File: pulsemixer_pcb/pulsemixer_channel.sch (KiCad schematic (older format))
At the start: 12 parts, among them SW501 Vol_Encoder, SW502 SW_MUTE, U501 MCP23017_SP

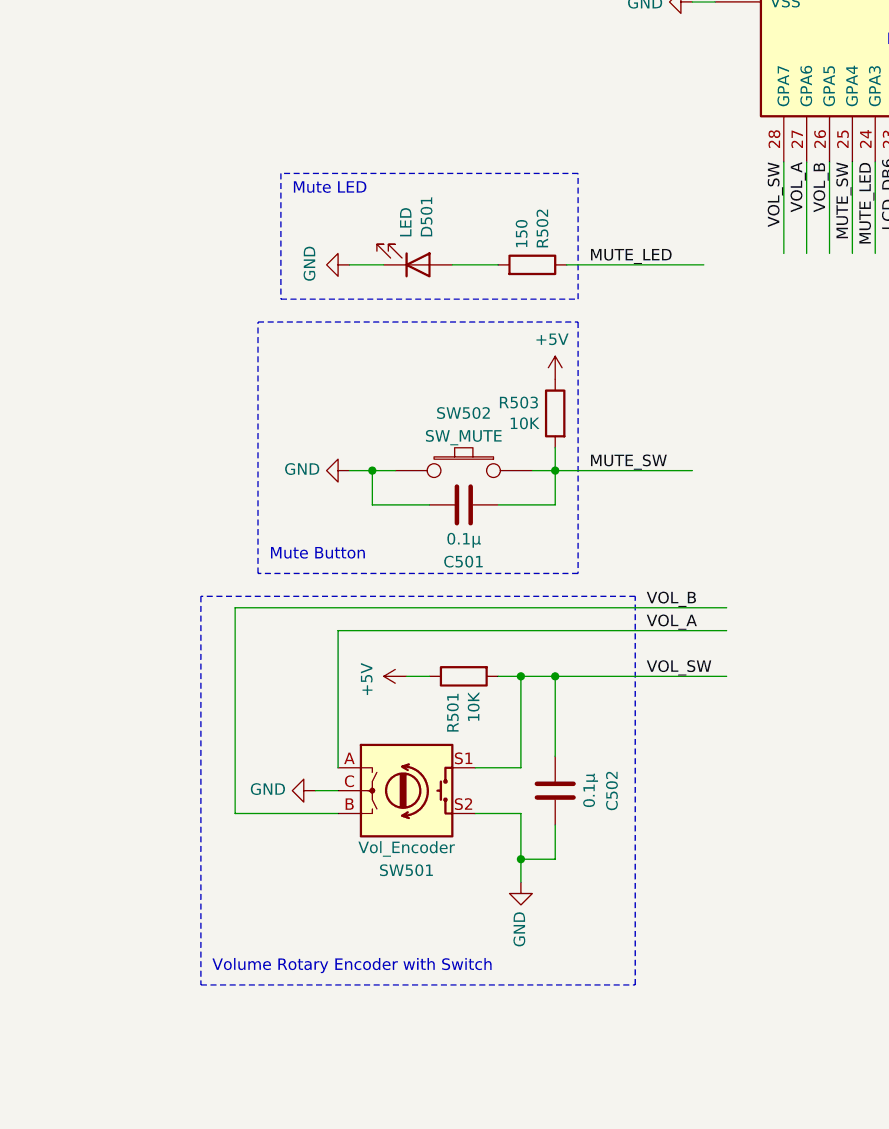
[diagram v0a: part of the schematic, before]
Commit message: Revised schematic after testing rotary encoder.
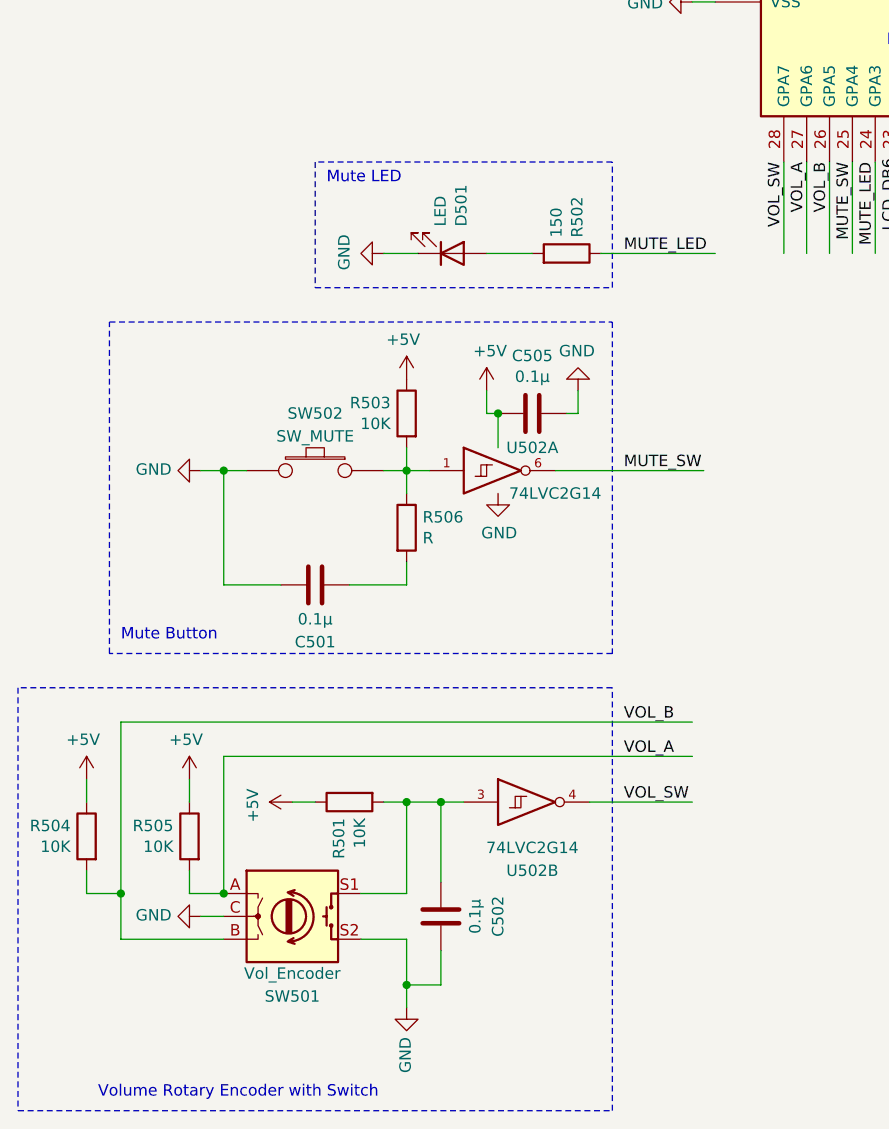
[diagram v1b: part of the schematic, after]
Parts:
- added C505: 0.1µ, symbol Device:C
- added R504, R505: 10K, Resistors_SMD:R_1206_HandSoldering, symbol Device:R
- added R506: R, symbol Device:R
- added U502: 74LVC2G14, symbol 74xGxx:74LVC2G14
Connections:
- wire segments 78 -> 93
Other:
- moved on the sheet: C501, C502, D501, R501, R502, R503, SW501, SW502

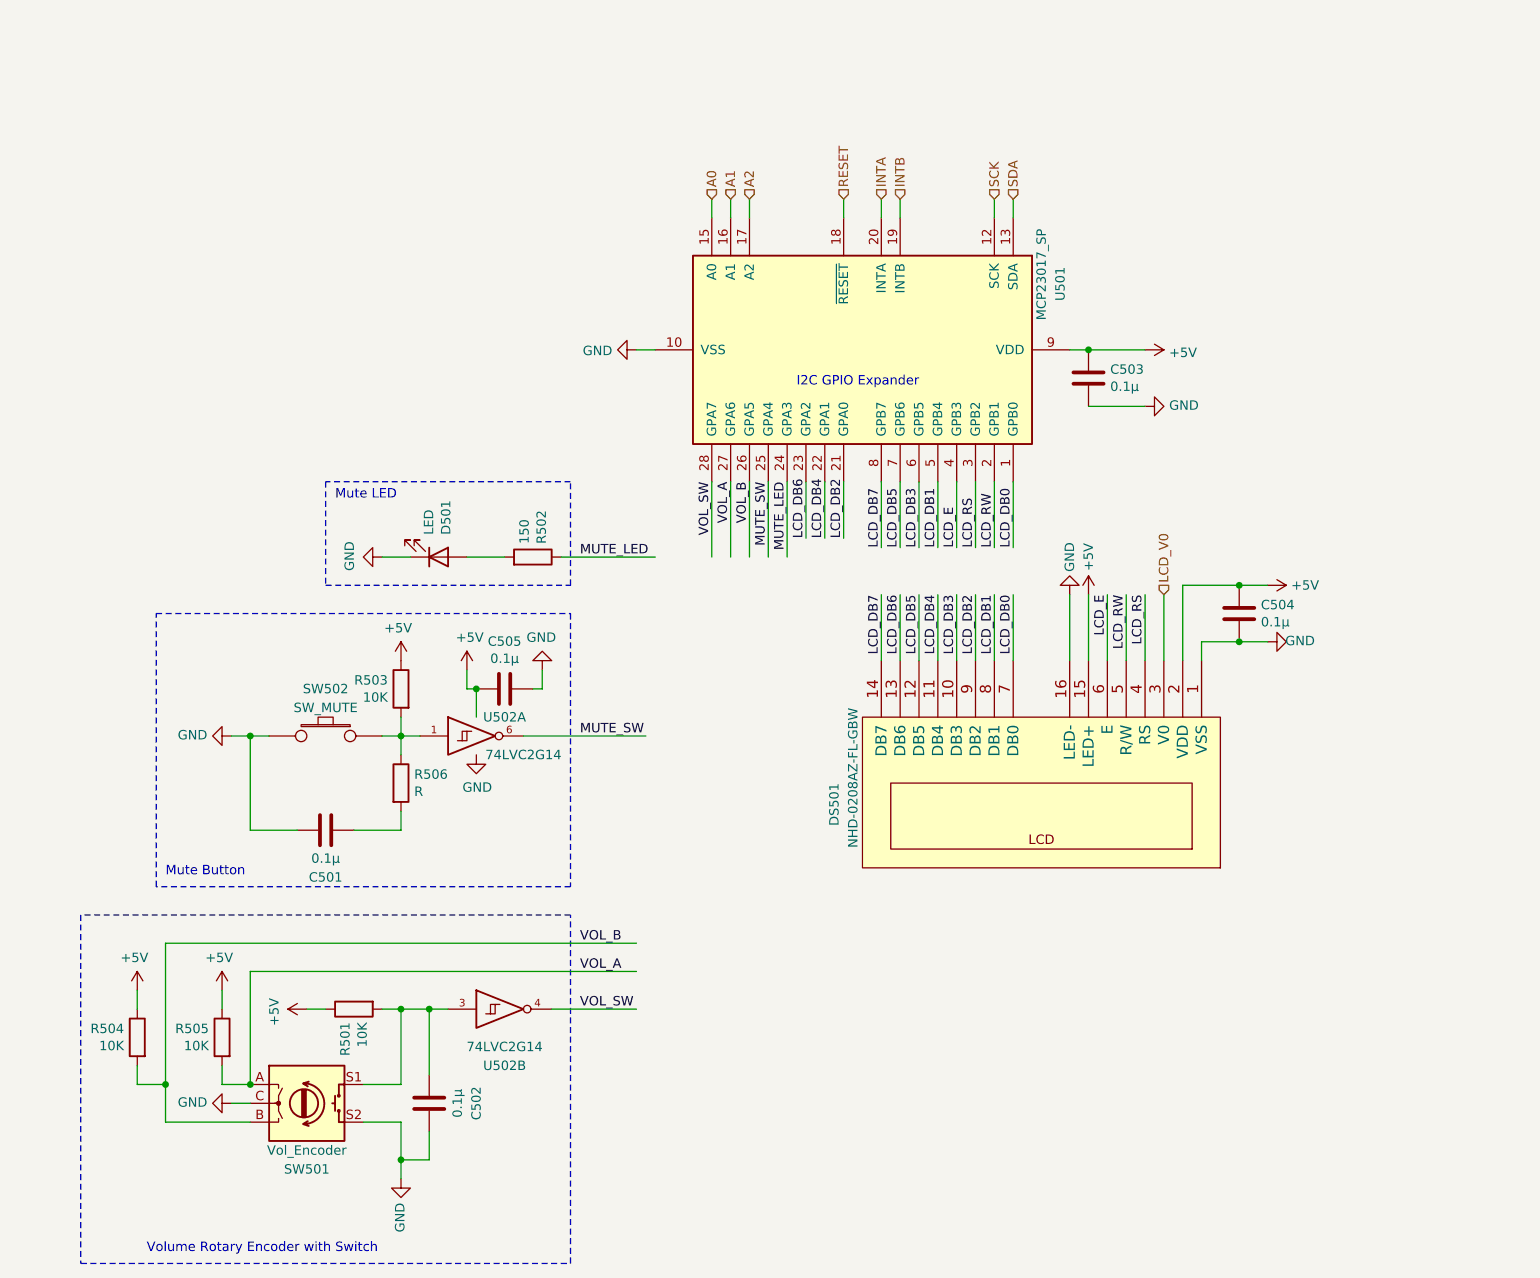
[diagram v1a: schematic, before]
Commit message: Simple reading of rotary encoder through the GPIO expander, with interrupts.
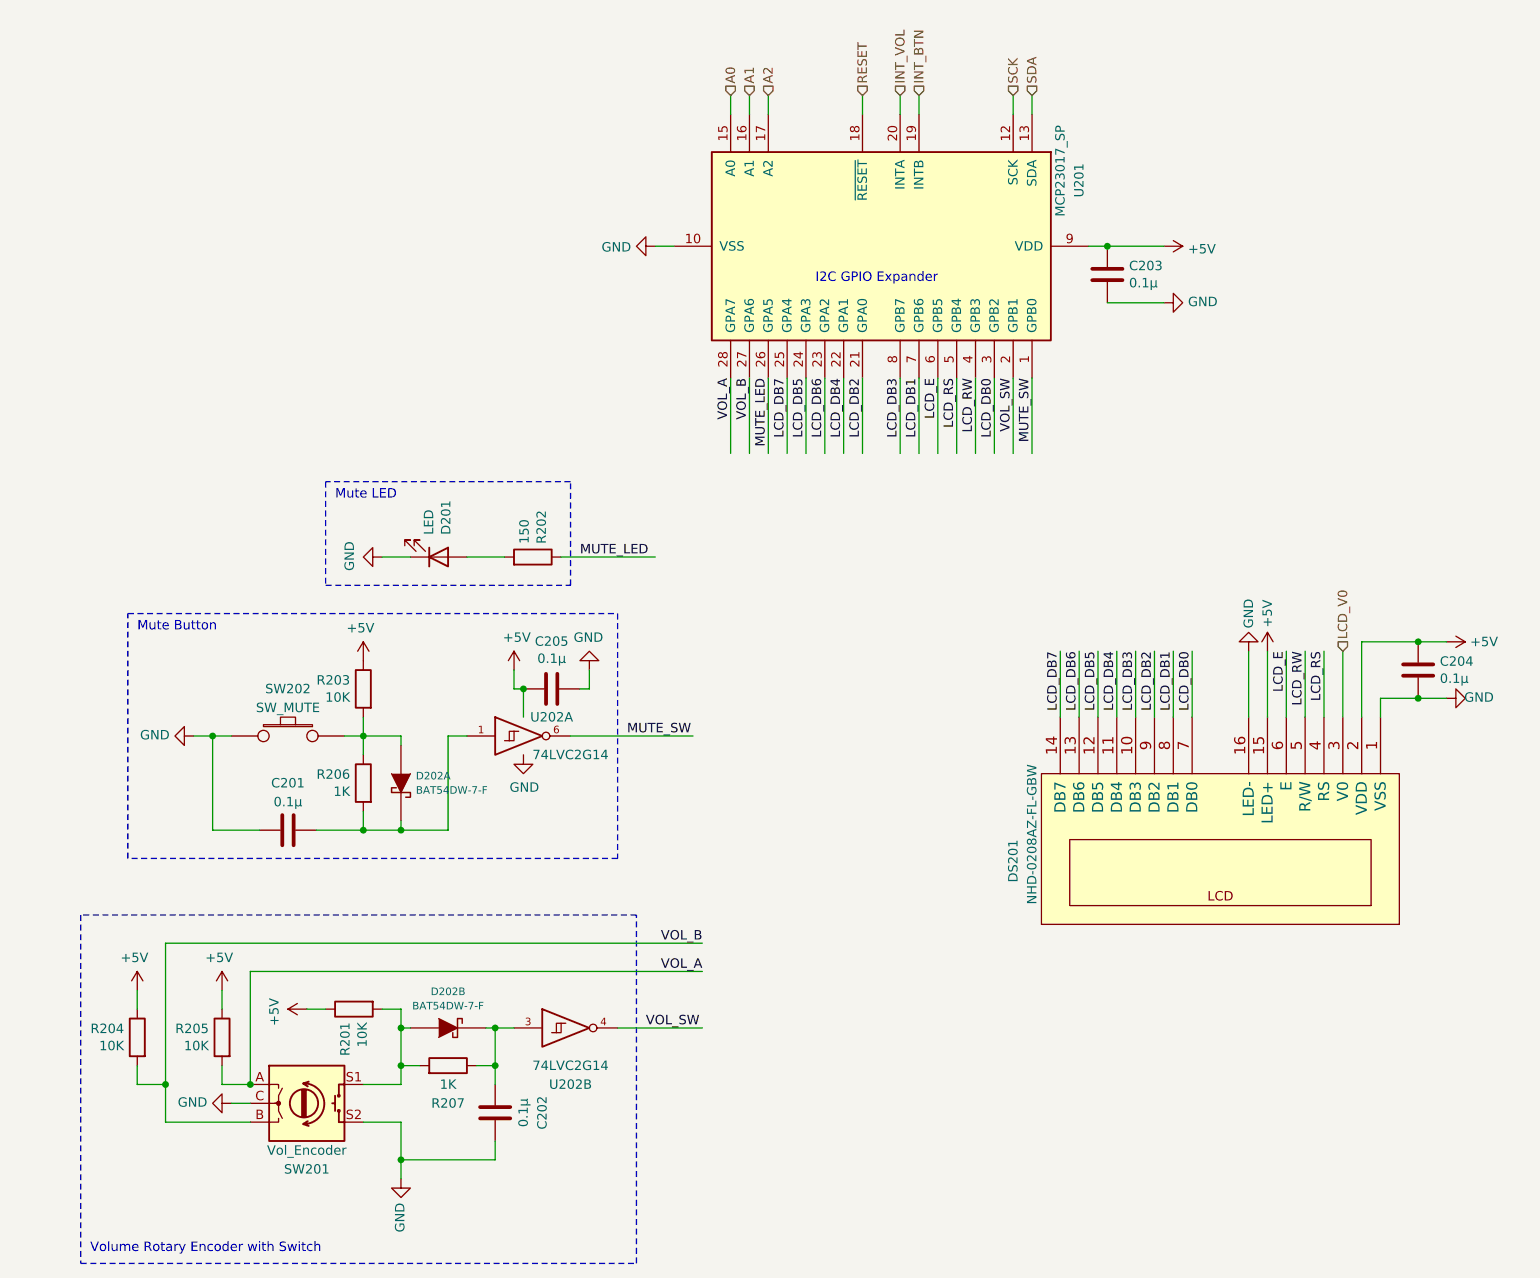
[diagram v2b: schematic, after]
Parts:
- added D502: BAT54DW-7-F, TO_SOT_Packages_SMD:SOT-23-6_Handsoldering, symbol pulsemixer_pcb:BAT54DW-7-F
- added R507: 1K, Resistors_SMD:R_1206_HandSoldering, symbol Device:R
- C505: footprint (none) -> Capacitors_SMD:C_0805_HandSoldering
- R506: value R -> 1K; footprint (none) -> Resistors_SMD:R_1206_HandSoldering
- U502: footprint (none) -> TO_SOT_Packages_SMD:SOT-23-6_Handsoldering
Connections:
- net labels added: INT_BTN, INT_VOL
- net labels removed: INTA, INTB
- wire segments 93 -> 105
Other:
- moved on the sheet: C201, C202, C203, C204, C205, DS201, R203, R206, SW202, U201, U202A, U202B

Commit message: Rearranged LCD pins to allow for interrupts on both GPIO banks.
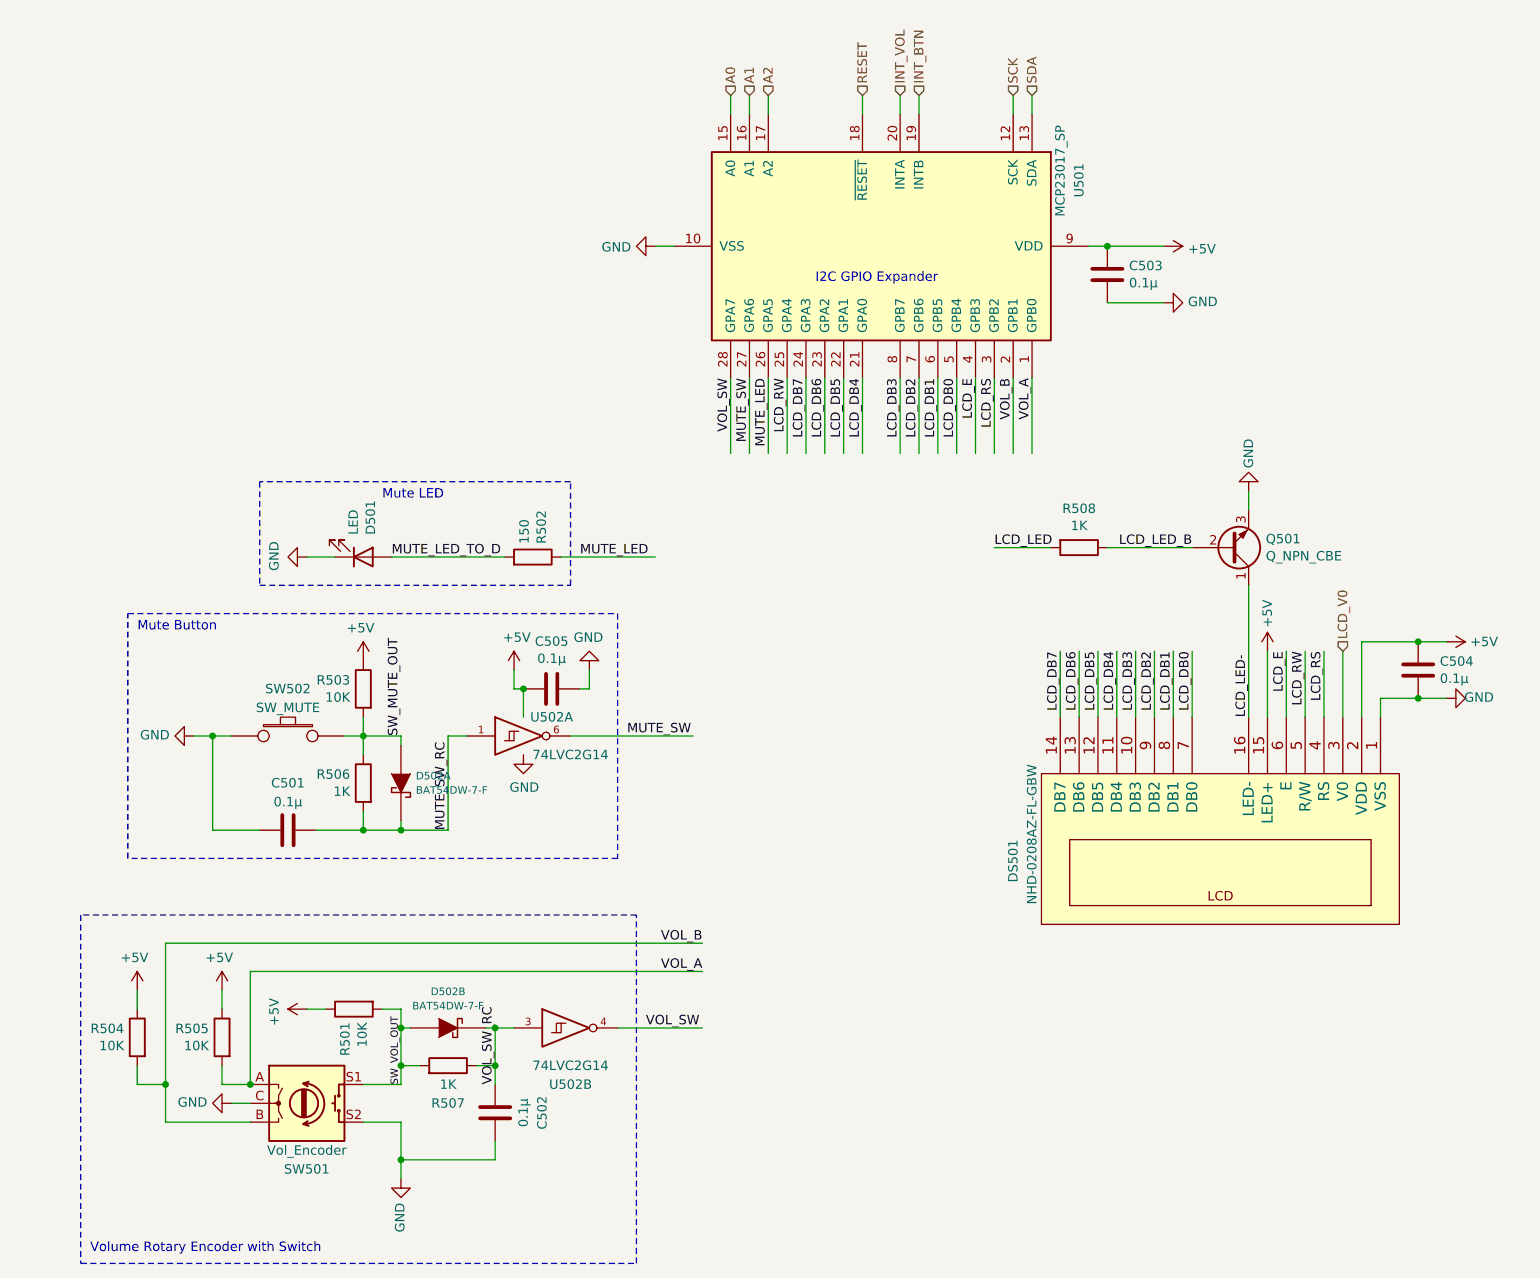
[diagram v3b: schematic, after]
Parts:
- added Q501: Q_NPN_CBE, TO_SOT_Packages_SMD:SOT-23_Handsoldering, symbol Device:Q_NPN_CBE
- added R508: 1K, Resistors_SMD:R_1206_HandSoldering, symbol Device:R
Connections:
- net labels added: LCD_LED, LCD_LED-, LCD_LED_B, MUTE_LED_TO_D, MUTE_SW_RC, SW_MUTE_OUT, SW_VOL_OUT, VOL_SW_RC
- wire segments 105 -> 108
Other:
- moved on the sheet: D501

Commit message: Firmware code to turn LCD backlight on and off.
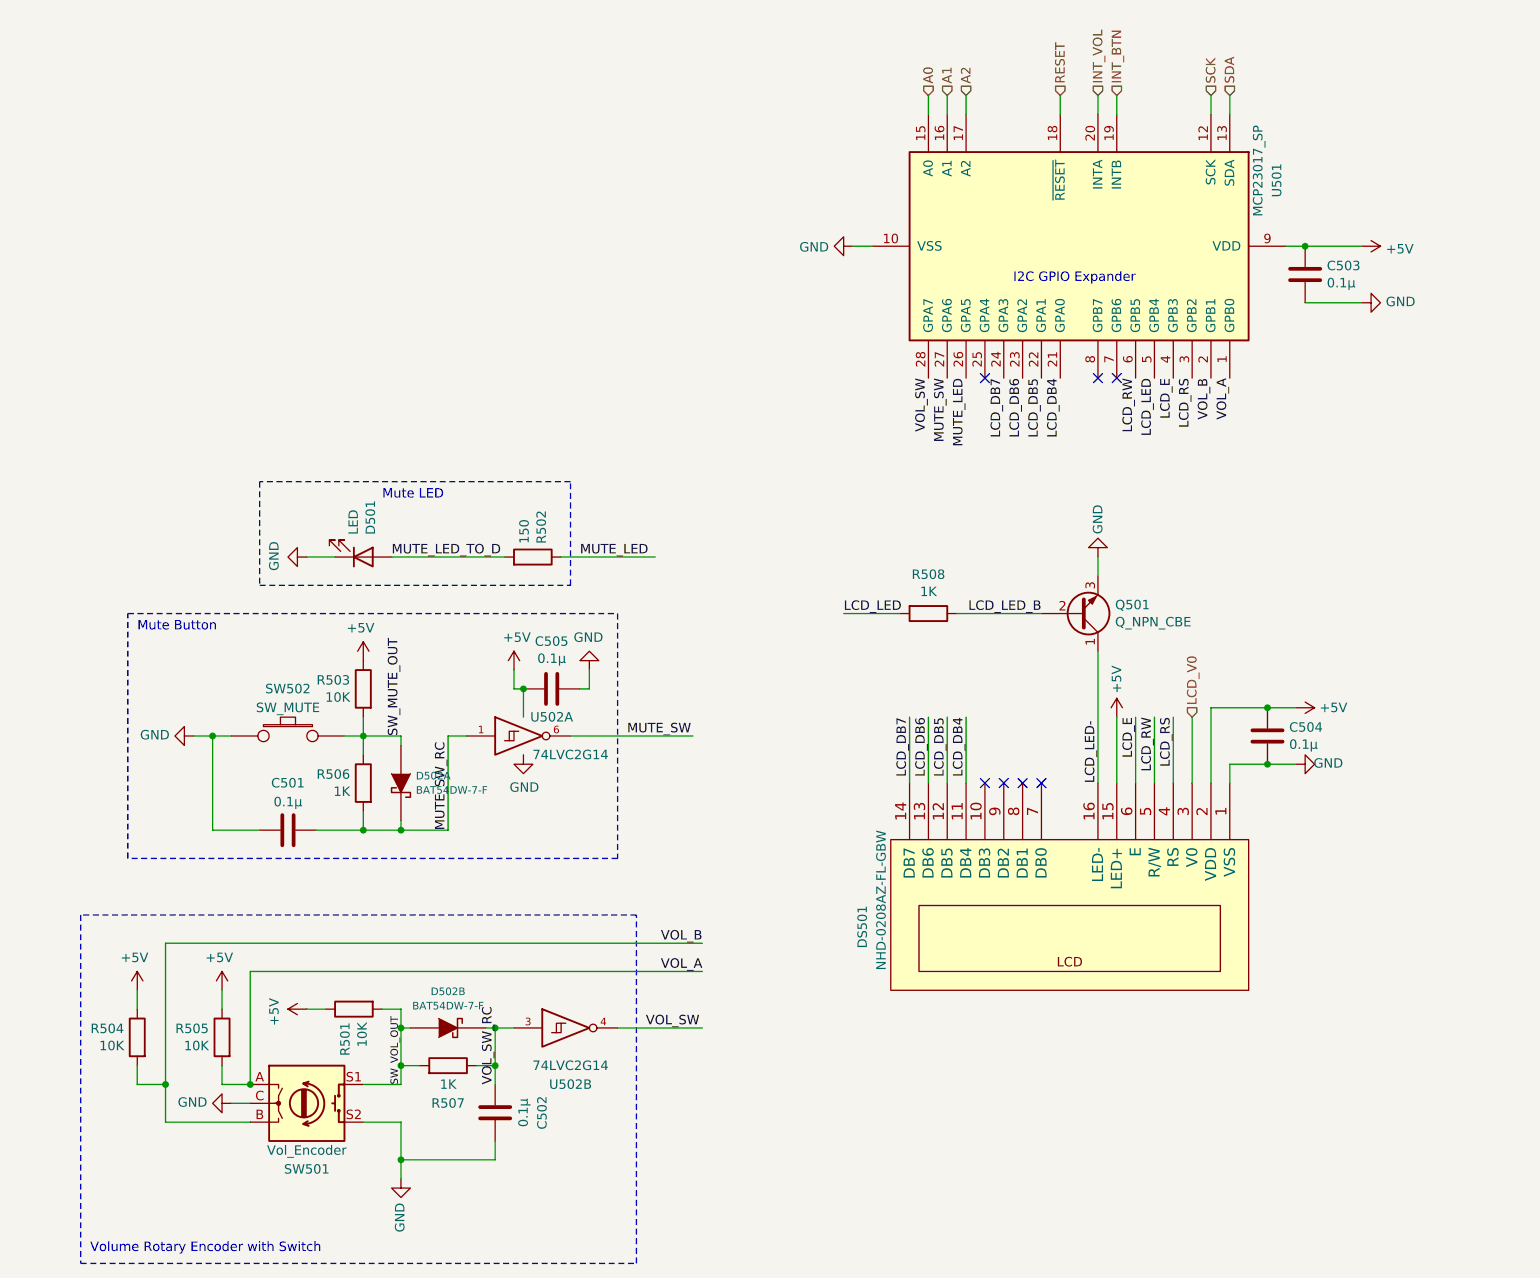
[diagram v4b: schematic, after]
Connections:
- net labels removed: LCD_DB0, LCD_DB1, LCD_DB2, LCD_DB3
- wire segments 108 -> 88
- no-connect marks 0 -> 7
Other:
- moved on the sheet: C503, C504, DS501, Q501, R508, U501

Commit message: Finished full PCB layout.
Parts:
- removed Q501: Q_NPN_CBE, TO_SOT_Packages_SMD:SOT-23_Handsoldering, symbol Device:Q_NPN_CBE
- removed U502: 74LVC2G14, TO_SOT_Packages_SMD:SOT-23-6_Handsoldering, symbol 74xGxx:74LVC2G14
- added Q201: Q_NPN_BEC, TO_SOT_Packages_SMD:SOT-23, symbol Device:Q_NPN_BEC
- added U502: 74LVC2G17, TO_SOT_Packages_SMD:SOT-23-6, symbol 74xGxx:74LVC2G17
- D501: value LED -> LED_RED
- D502: footprint TO_SOT_Packages_SMD:SOT-23-6_Handsoldering -> pulsemixer_pcb:Diode_Dual_SOT-23-6
- R501, R502, R503, R504, R505, R506, R507, R508: footprint Resistors_SMD:R_1206_HandSoldering -> Resistors_SMD:R_1206
- SW502: value SW_MUTE -> SW_PUSH_SPST
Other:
- moved on the sheet: C201, C202, C203, C204, C205, D201, D202A, D202B, DS201, R201, R202, R203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
